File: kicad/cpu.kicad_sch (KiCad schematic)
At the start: 8 parts, among them U3 W65C02SxP

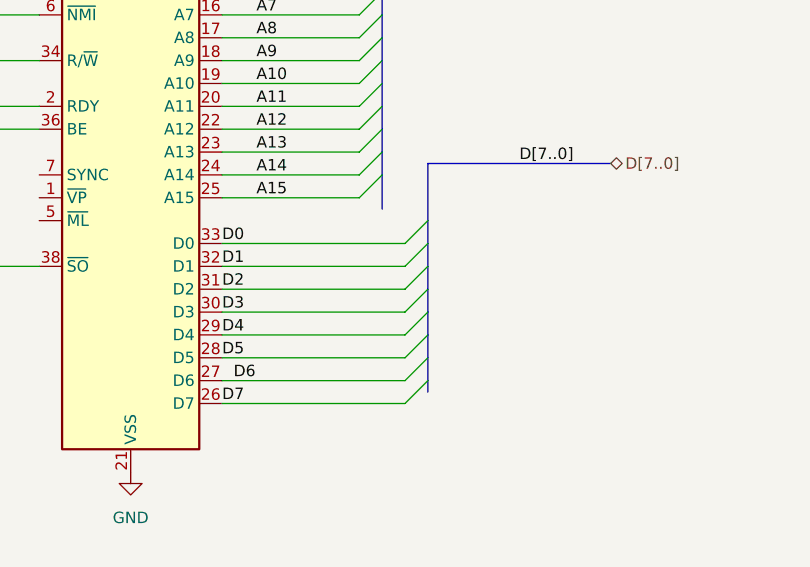
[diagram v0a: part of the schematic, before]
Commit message: start of rev3, reduce x-size, leds consistent
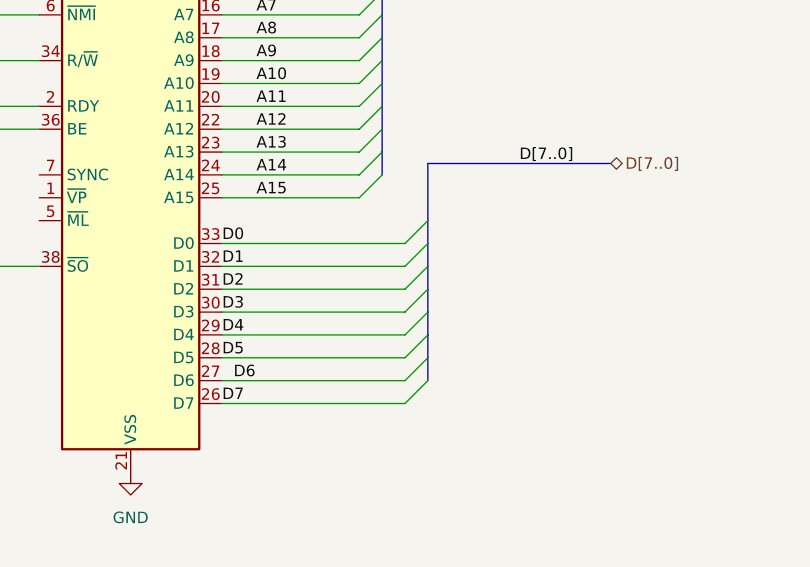
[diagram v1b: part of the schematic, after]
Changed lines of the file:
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@@
-		)
-	)
-	(bus
-		(pts
-			(xy 118.11 82.55) (xy 118.11 86.36)
-		)
-		(stroke
-			(width 0)
-			(type default)
 		)
 	)
@@
 		)
 		(stroke
-			(width 0)
-			(type default)
-		)
-	)
-	(bus
-		(pts
-			(xy 123.19 105.41) (xy 123.19 106.68)
-		)
-		(stroke
